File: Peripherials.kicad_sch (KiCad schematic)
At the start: 27 parts, among them J1 esp32 left side, J12 USB_C_Receptacle_USB2.0_14P, J14 IDC_Cable_02x08, J15 Conn_01x02_Pin, J18 Micro_SD_Card, J2 esp32 right side, Q2 NMOS, U12 USBLC6-2P6, U2 RV-3028-C7

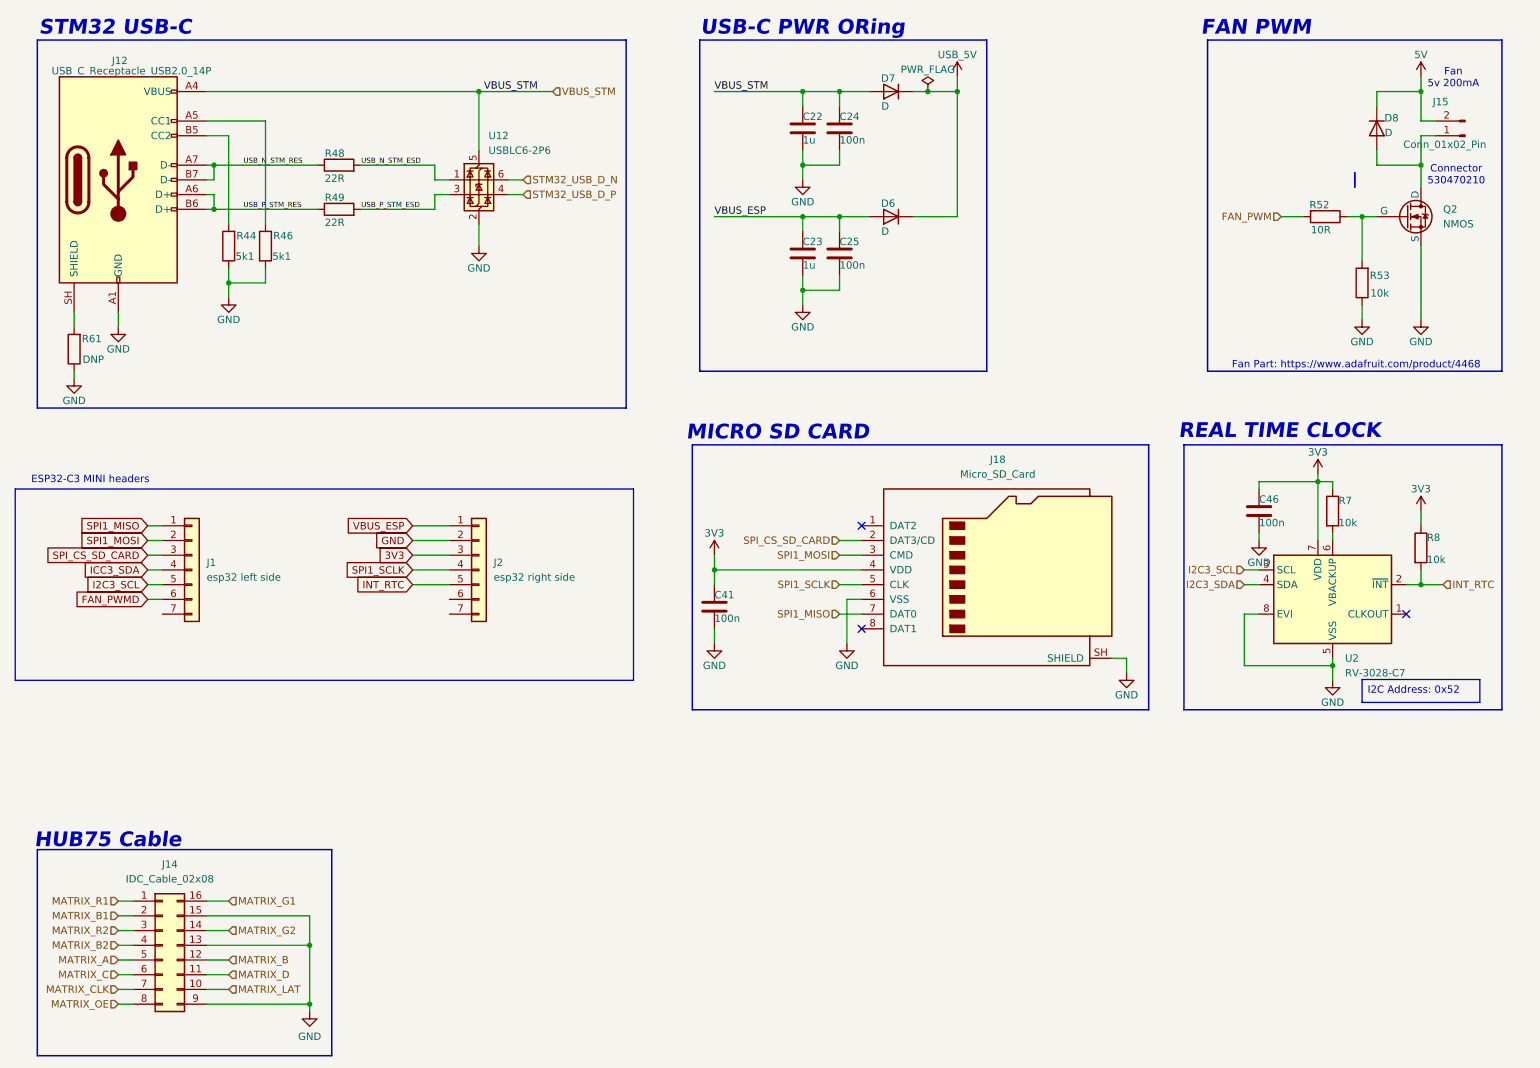
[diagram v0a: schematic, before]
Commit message: got rid of pins on stm32
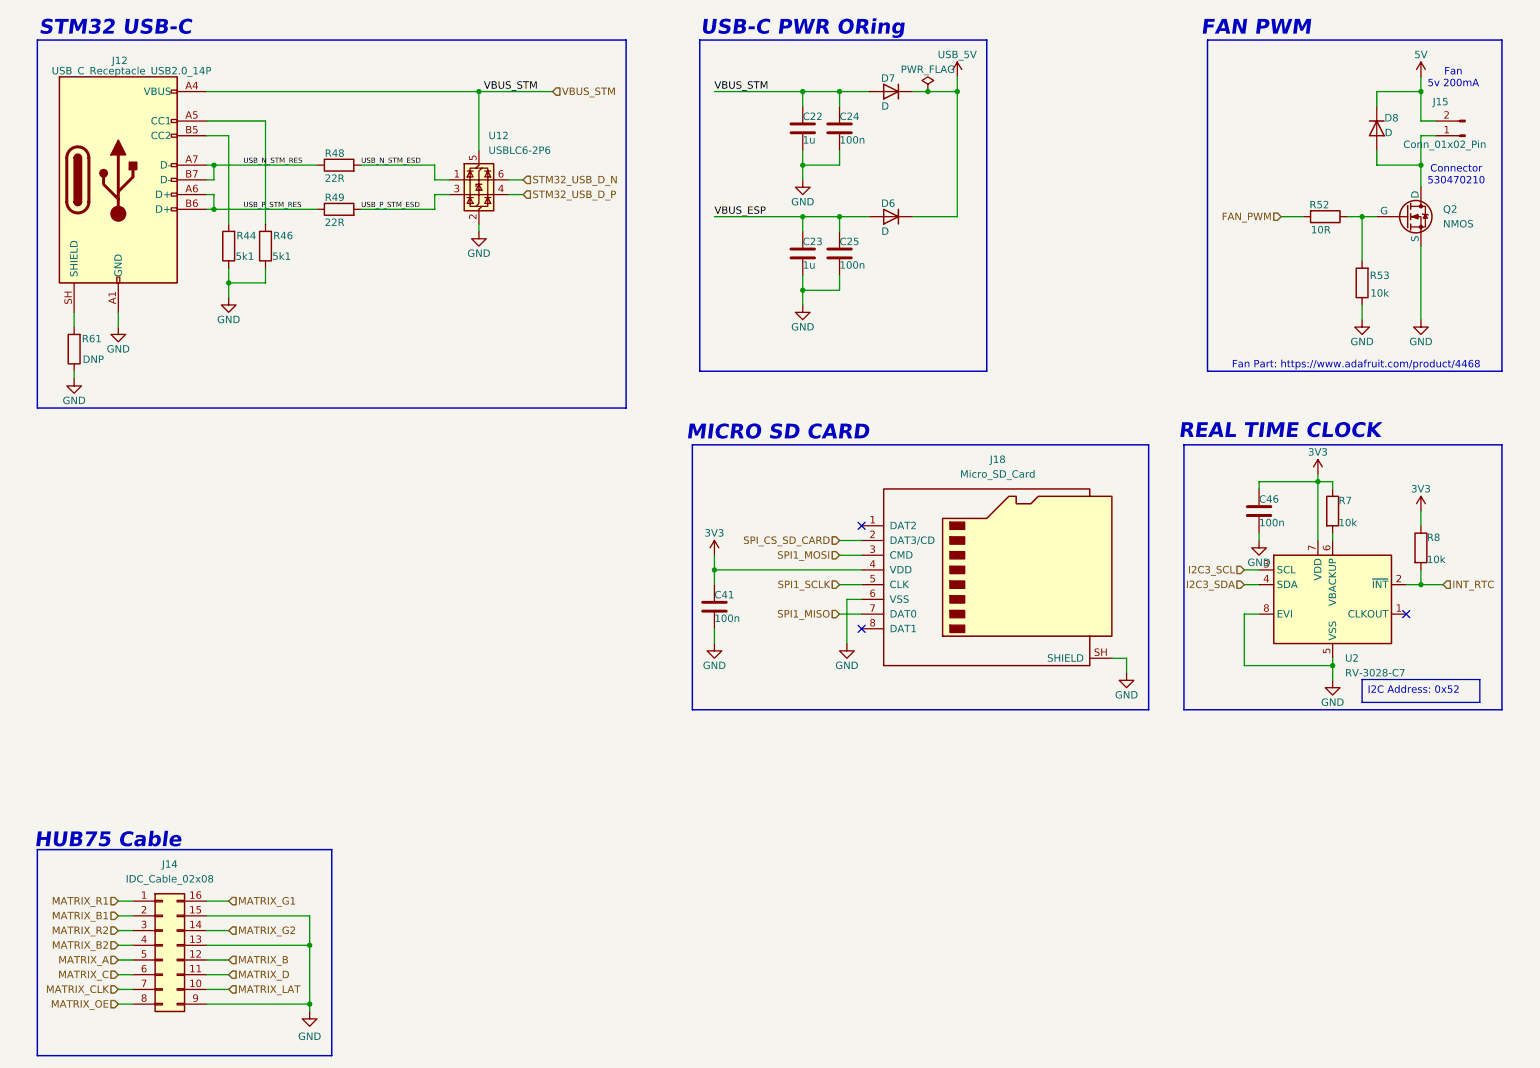
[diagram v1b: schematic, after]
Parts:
- removed J1: esp32 left side, symbol Connector_Generic:Conn_01x07
- removed J2: esp32 right side, symbol Connector_Generic:Conn_01x07
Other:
- note removed: "ESP32-C3 MINI headers"
